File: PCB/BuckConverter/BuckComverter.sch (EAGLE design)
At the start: 34 parts, among them IC1 LP2950CDT-3.3

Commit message: テストパッドを追加
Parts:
- added PAD1, PAD2, PAD3, PAD4: (no value), wirepad:1,6/0,8
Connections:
- net +12V: now also PAD2.P
- net GND: now also PAD1.P
- net IC_SIG_5V: now also PAD4.P
- net VA_IN: now also PAD3.P
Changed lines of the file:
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@@
 <?xml version="1.0" encoding="utf-8"?>
 <!DOCTYPE eagle SYSTEM "eagle.dtd">
-<eagle version="7.2.0">
+<eagle version="7.5.0">
 <drawing>
 <settings>
@@
 <layers>
 <layer number="1" name="Top" color="4" fill="1" visible="no" active="no"/>
+<layer number="2" name="Route2" color="1" fill="3" visible="no" active="no"/>
+<layer number="3" name="Route3" color="4" fill="3" visible="no" active="no"/>
+<layer number="14" name="Route14" color="1" fill="6" visible="no" active="no"/>
+<layer number="15" name="Route15" color="4" fill="6" visible="no" active="no"/>
 <layer number="16" name="Bottom" color="1" fill="1" visible="no" active="no"/>
 <layer number="17" name="Pads" color="2" fill="1" visible="no" active="no"/>
@@
 <part name="R_LED2" library="rcl" deviceset="R-US_" device="0204/5" value="4.7k"/>
 <part name="SUPPLY16" library="supply2" deviceset="GND" device=""/>
+<part name="PAD1" library="wirepad" deviceset="1,6/0,8" device=""/>
+<part name="PAD2" library="wirepad" deviceset="1,6/0,8" device=""/>
+<part name="SUPPLY17" library="supply2" deviceset="GND" device=""/>
+<part name="SUPPLY18" library="supply2" deviceset="+12V" device=""/>
+<part name="PAD3" library="wirepad" deviceset="1,6/0,8" device=""/>
+<part name="PAD4" library="wirepad" deviceset="1,6/0,8" device=""/>
 </parts>
 <sheets>
@@
 <instance part="R_LED2" gate="G$1" x="38.1" y="-114.3" rot="R90"/>
 <instance part="SUPPLY16" gate="GND" x="38.1" y="-129.54"/>
+<instance part="PAD1" gate="P" x="152.4" y="43.18" rot="R180"/>
+<instance part="PAD2" gate="P" x="152.4" y="50.8" rot="R180"/>
+<instance part="SUPPLY17" gate="GND" x="142.24" y="40.64"/>
+<instance part="SUPPLY18" gate="+12V" x="142.24" y="53.34"/>
+<instance part="PAD3" gate="P" x="-35.56" y="5.08" rot="R270"/>
+<instance part="PAD4" gate="P" x="53.34" y="5.08" rot="R270"/>
 </instances>
 <busses>
@@
 <wire x1="-35.56" y1="-43.18" x2="-25.4" y2="-43.18" width="0.1524" layer="91"/>
 <junction x="-35.56" y="-43.18"/>
+</segment>
+<segment>
+<pinref part="SUPPLY18" gate="+12V" pin="+12V"/>
+<pinref part="PAD2" gate="P" pin="P"/>
+<wire x1="142.24" y1="50.8" x2="149.86" y2="50.8" width="0.1524" layer="91"/>
 </segment>
 </net>
@@
 <pinref part="LED2" gate="G$1" pin="C"/>
 </segment>
+<segment>
+<pinref part="PAD1" gate="P" pin="P"/>
+<pinref part="SUPPLY17" gate="GND" pin="GND"/>
+<wire x1="149.86" y1="43.18" x2="142.24" y2="43.18" width="0.1524" layer="91"/>
+</segment>
 </net>
 <net name="N$5" class="0">
@@
 <segment>
 <pinref part="R_5V" gate="G$1" pin="1"/>
-<wire x1="58.42" y1="0" x2="33.02" y2="0" width="0.1524" layer="91"/>
+<wire x1="58.42" y1="0" x2="53.34" y2="0" width="0.1524" layer="91"/>
 <label x="27.94" y="0" size="1.778" layer="95" rot="R180" xref="yes"/>
 <pinref part="JP1" gate="1" pin="1"/>
+<wire x1="53.34" y1="0" x2="33.02" y2="0" width="0.1524" layer="91"/>
 <wire x1="33.02" y1="0" x2="27.94" y2="0" width="0.1524" layer="91"/>
 <wire x1="33.02" y1="17.78" x2="33.02" y2="0" width="0.1524" layer="91"/>
 <junction x="33.02" y="0"/>
+<pinref part="PAD4" gate="P" pin="P"/>
+<wire x1="53.34" y1="2.54" x2="53.34" y2="0" width="0.1524" layer="91"/>
 </segment>
 </net>
@@
 <wire x1="-27.94" y1="-2.54" x2="-35.56" y2="-2.54" width="0.1524" layer="91"/>
 <junction x="-27.94" y="-2.54"/>
-</segment>
-<segment>
+<pinref part="PAD3" gate="P" pin="P"/>
+<wire x1="-35.56" y1="2.54" x2="-35.56" y2="-2.54" width="0.1524" layer="91"/>
+</segment>
+<segment>

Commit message: 穴径を0.8, 1.0, 1.5, 3.2mmに統一
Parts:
- added PAD5: (no value), wirepad:1,6/0,8
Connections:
- net VOUT: now also PAD5.P
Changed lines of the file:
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@@
 <part name="PAD3" library="wirepad" deviceset="1,6/0,8" device=""/>
 <part name="PAD4" library="wirepad" deviceset="1,6/0,8" device=""/>
+<part name="PAD5" library="wirepad" deviceset="1,6/0,8" device=""/>
 </parts>
 <sheets>
@@
 <instance part="PAD3" gate="P" x="-35.56" y="5.08" rot="R270"/>
 <instance part="PAD4" gate="P" x="53.34" y="5.08" rot="R270"/>
+<instance part="PAD5" gate="P" x="81.28" y="60.96" rot="R270"/>
 </instances>
 <busses>
@@
 <pinref part="OUTPUT" gate="-2" pin="KL"/>
 <wire x1="96.52" y1="55.88" x2="109.22" y2="55.88" width="0.1524" layer="91"/>
-</segment>
-<segment>
+<pinref part="PAD5" gate="P" pin="P"/>
+<wire x1="81.28" y1="58.42" x2="81.28" y2="55.88" width="0.1524" layer="91"/>
+</segment>
+<segment>

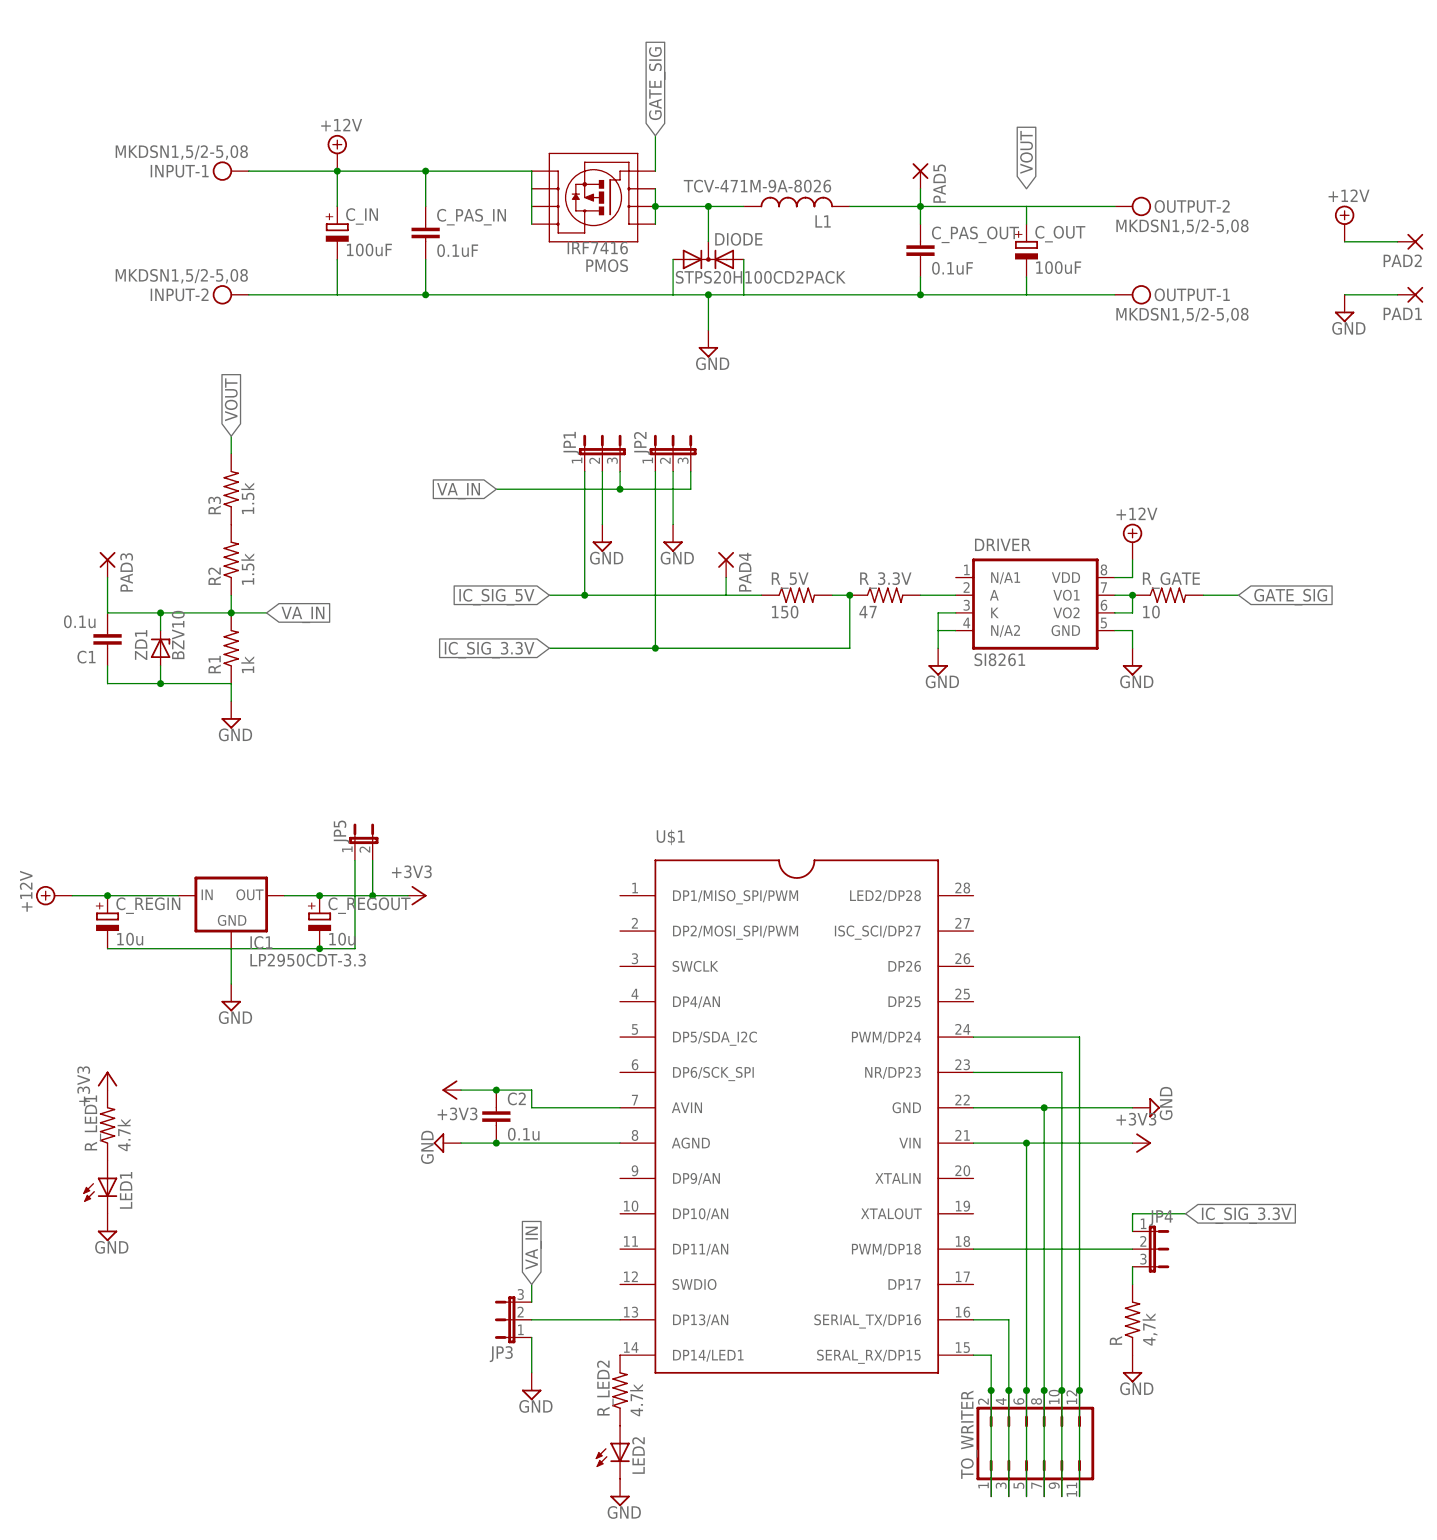
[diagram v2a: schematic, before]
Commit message: 回路のミスを修正
修正内容：
レギュレータのピン配置を修正
PMOSの配線を修正
上記に伴い、パターンの再設計
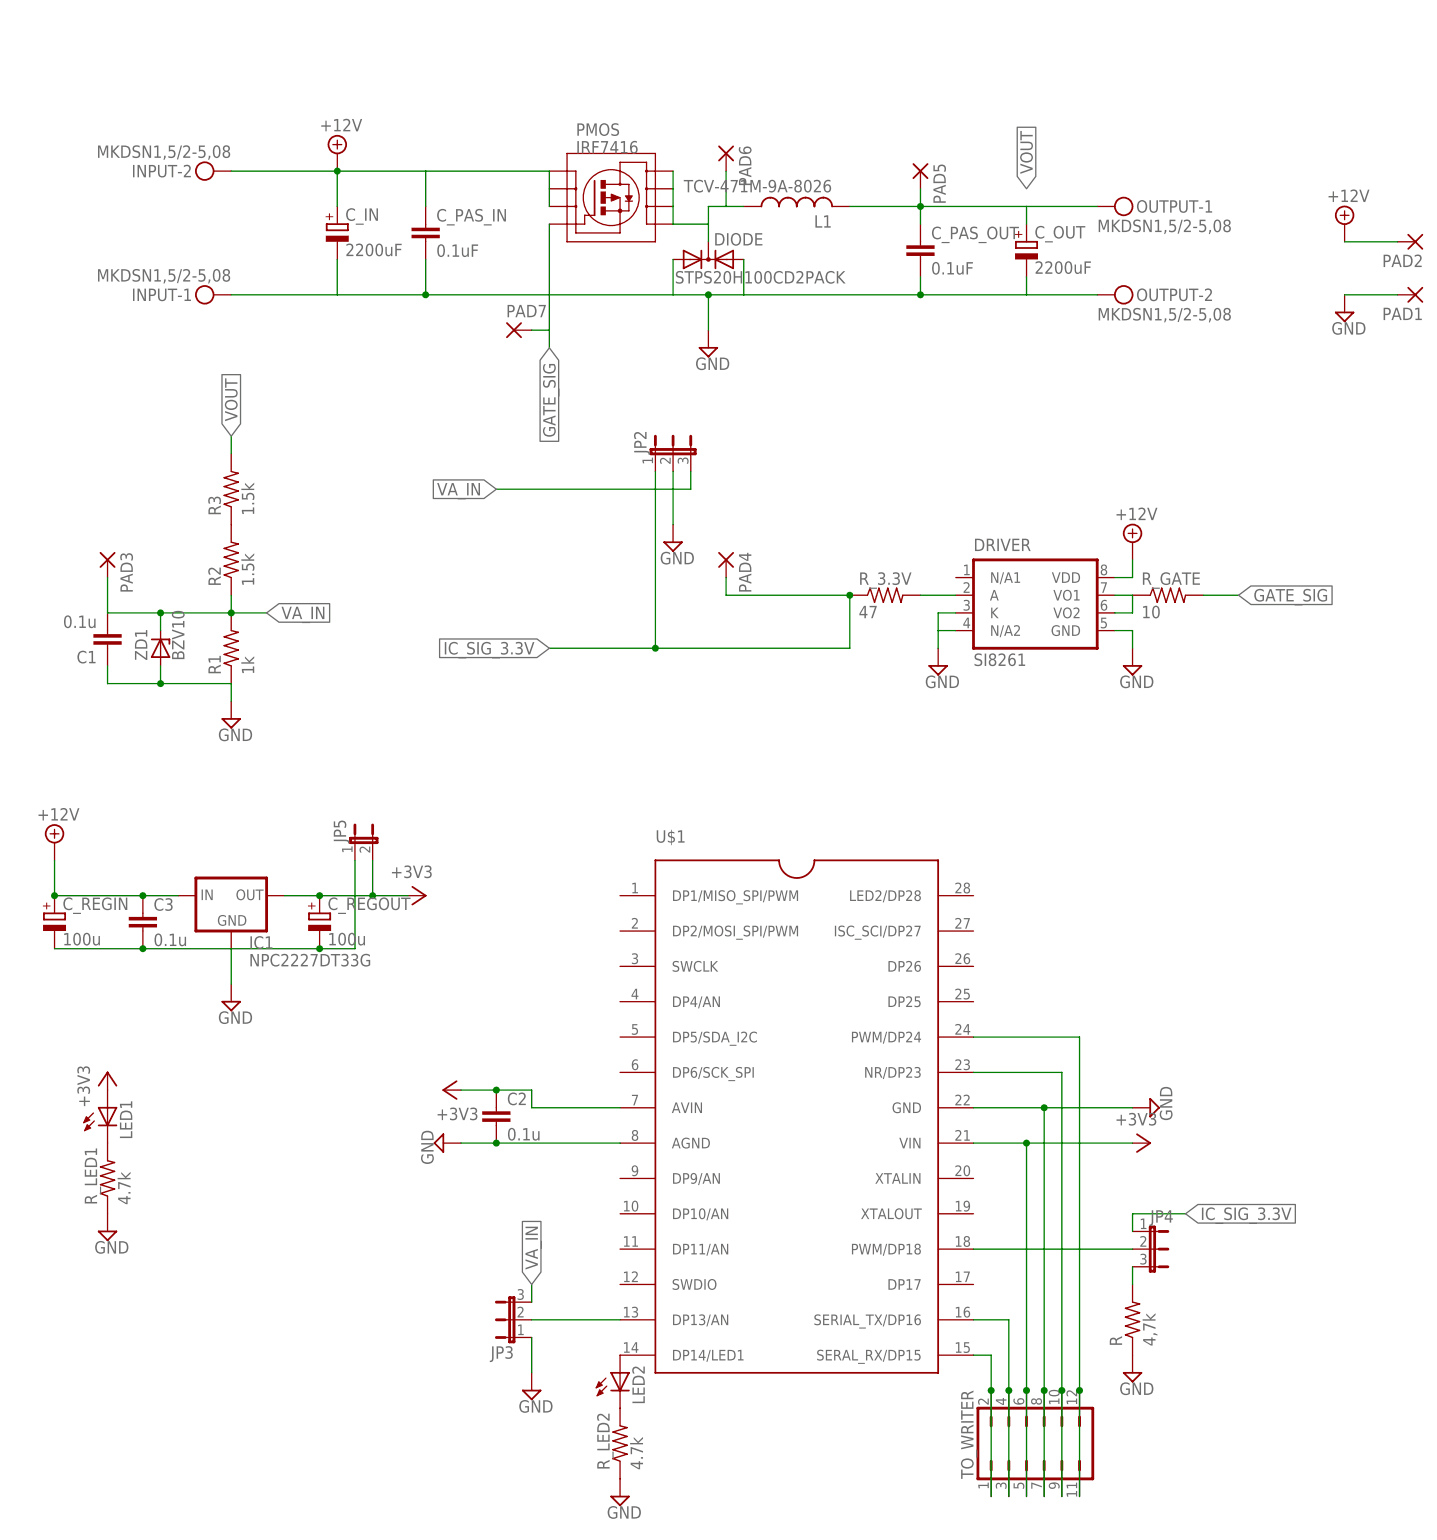
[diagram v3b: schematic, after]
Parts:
- removed JP1: (no value), jumper:JP2E
- removed R_5V: 150, rcl:R-US_0207/2V
- added C3: 0.1u, rcl:C-EU025-024X044
- added PAD6, PAD7: (no value), wirepad:1,6/0,8
- C_IN, C_OUT: value 100uF -> 2200uF; device rcl:CPOL-EUE2.5-7 -> rcl:CPOL-EUE7.5-16
- C_REGIN, C_REGOUT: value 10u -> 100u
- IC1: value LP2950CDT-3.3 -> NPC2227DT33G; device v-reg:LP2950CDT-3.3 -> v-reg2:NPC2227DT33G
- R_LED1: device rcl:R-US_0204/5 -> rcl:R-US_0204/2V
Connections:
- removed net IC_SIG_5V: JP1.1, PAD4.P, R_5V.1
- removed net N$14: LED2.A, R_LED2.1
- new net N$19: DIODE.C, L1.1, PAD6.P, PMOS.D5, PMOS.D6, PMOS.D7, PMOS.D8
- net +12V: now also C3.1, INPUT-2.KL, PMOS.S1, PMOS.S2, PMOS.S3; no longer INPUT-1.KL, PMOS.D5, PMOS.D6, PMOS.D7, PMOS.D8
- net +3V3: now also LED1.A; no longer R_LED1.2
- net GATE_SIG: now also PAD7.P
- net GND: now also C3.2, INPUT-1.KL, OUTPUT-2.KL, R_LED1.1, R_LED2.1; no longer INPUT-2.KL, JP1.2, LED1.C, LED2.C, OUTPUT-1.KL
- net IC_SIG_3.3V: now also PAD4.P; no longer R_5V.2
- net N$1: now also LED1.C, R_LED1.2; no longer DIODE.C, L1.1, PMOS.S1, PMOS.S2, PMOS.S3
- net N$13: now also LED2.C; no longer U$1.DP14/LED1
- net N$3: now also LED2.A, U$1.DP14/LED1; no longer LED1.A, R_LED1.1
- net VA_IN: no longer JP1.3
- net VOUT: now also OUTPUT-1.KL; no longer OUTPUT-2.KL
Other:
- moved on the sheet: C_REGIN, INPUT-1, INPUT-2, LED1, LED2, OUTPUT-1, OUTPUT-2, PMOS, R_LED1, R_LED2

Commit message: 回路を改良
詳細:
殆どの信号線を0.016 -> 0.032 inch に変更
ゲート周りの回路の最適化
制御回路の電源ラインの最適化
一部パーツの形状を変更
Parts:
- R3: device rcl:R-US_0207/10 -> rcl:R-US_0207/7
- R_3.3V: device rcl:R-US_0207/2V -> rcl:R-US_0204/7
- R_LED2: device rcl:R-US_0204/5 -> rcl:R-US_0204/7
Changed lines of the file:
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@@
 <part name="SUPPLY5" library="supply2" deviceset="+12V" device=""/>
 <part name="SUPPLY1" library="supply2" deviceset="GND" device=""/>
-<part name="R_3.3V" library="rcl" deviceset="R-US_" device="0207/2V" value="47"/>
+<part name="R_3.3V" library="rcl" deviceset="R-US_" device="0204/7" value="47"/>
 <part name="OUTPUT" library="con-phoenix-508" deviceset="MKDSN1,5/2-5,08" device=""/>
 <part name="INPUT" library="con-phoenix-508" deviceset="MKDSN1,5/2-5,08" device=""/>
@@
 <part name="R1" library="rcl" deviceset="R-US_" device="0207/7" value="1k"/>
 <part name="SUPPLY8" library="supply2" deviceset="GND" device=""/>
-<part name="R3" library="rcl" deviceset="R-US_" device="0207/10" value="1.5k"/>
+<part name="R3" library="rcl" deviceset="R-US_" device="0207/7" value="1.5k"/>
 <part name="ZD1" library="diode" deviceset="BZV10" device=""/>
 <part name="LED1" library="led" deviceset="LED" device="3MM"/>
@@
 <part name="JP5" library="jumper" deviceset="JP1E" device=""/>
 <part name="LED2" library="led" deviceset="LED" device="3MM"/>
-<part name="R_LED2" library="rcl" deviceset="R-US_" device="0204/5" value="4.7k"/>
+<part name="R_LED2" library="rcl" deviceset="R-US_" device="0204/7" value="4.7k"/>
 <part name="SUPPLY16" library="supply2" deviceset="GND" device=""/>
 <part name="PAD1" library="wirepad" deviceset="1,6/0,8" device=""/>
